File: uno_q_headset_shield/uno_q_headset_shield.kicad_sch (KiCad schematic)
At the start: 4 parts, among them J1 Power, J2 Digital/PWM, J3 Analog, J4 Digital/PWM

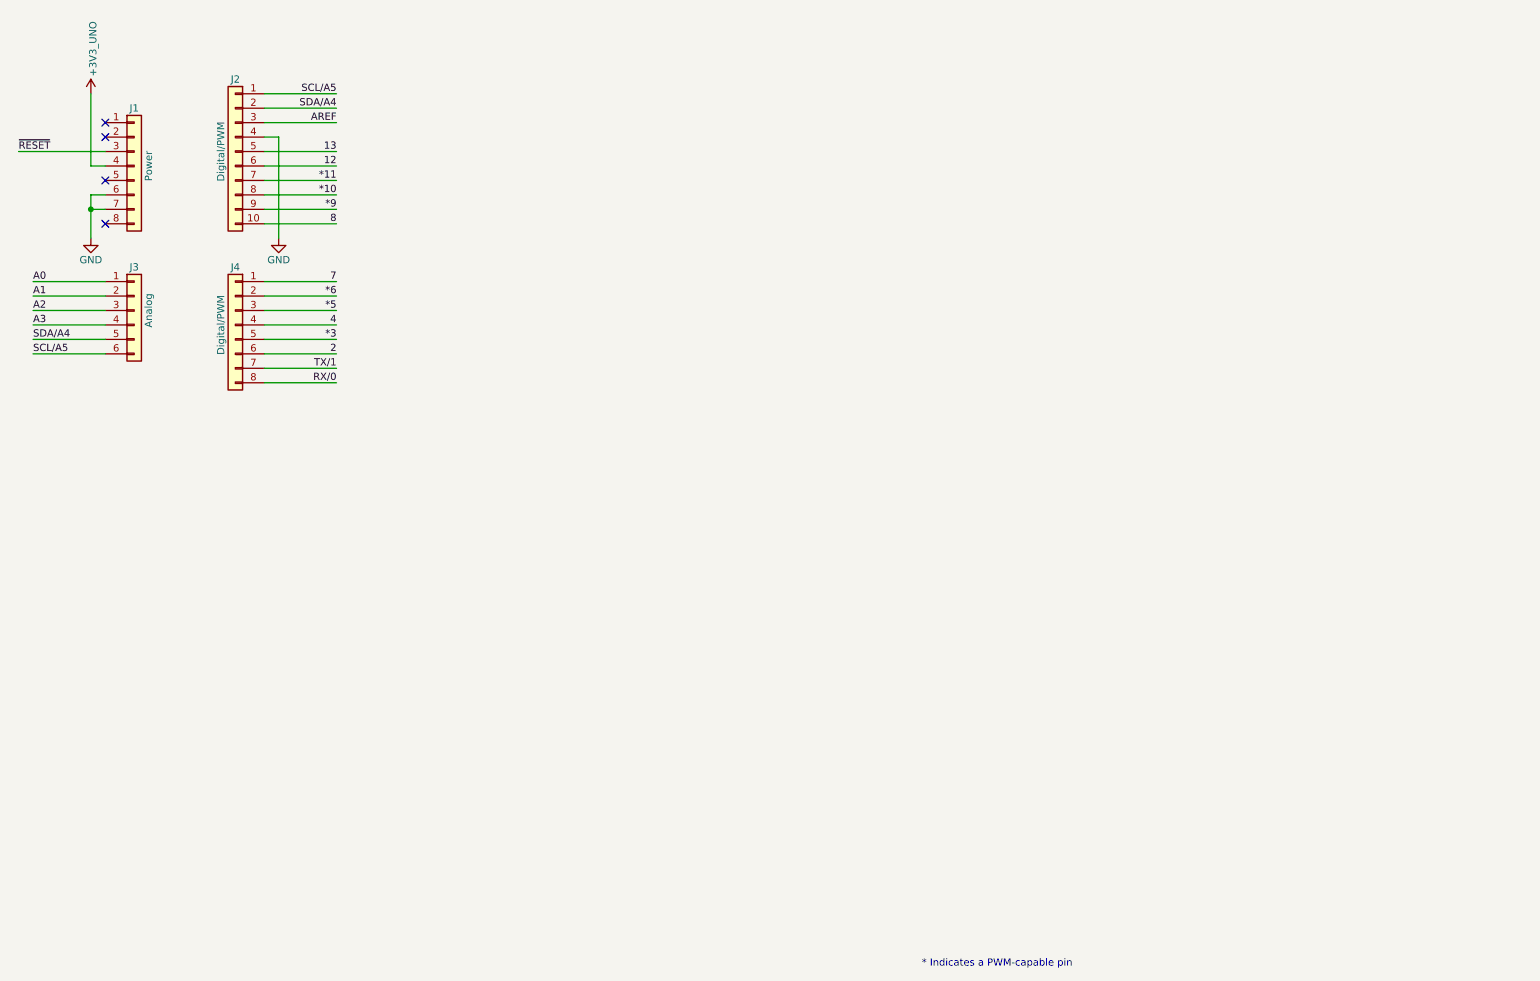
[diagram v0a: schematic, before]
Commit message: Full first pass at schematic (still need to finalize digital pin selection)
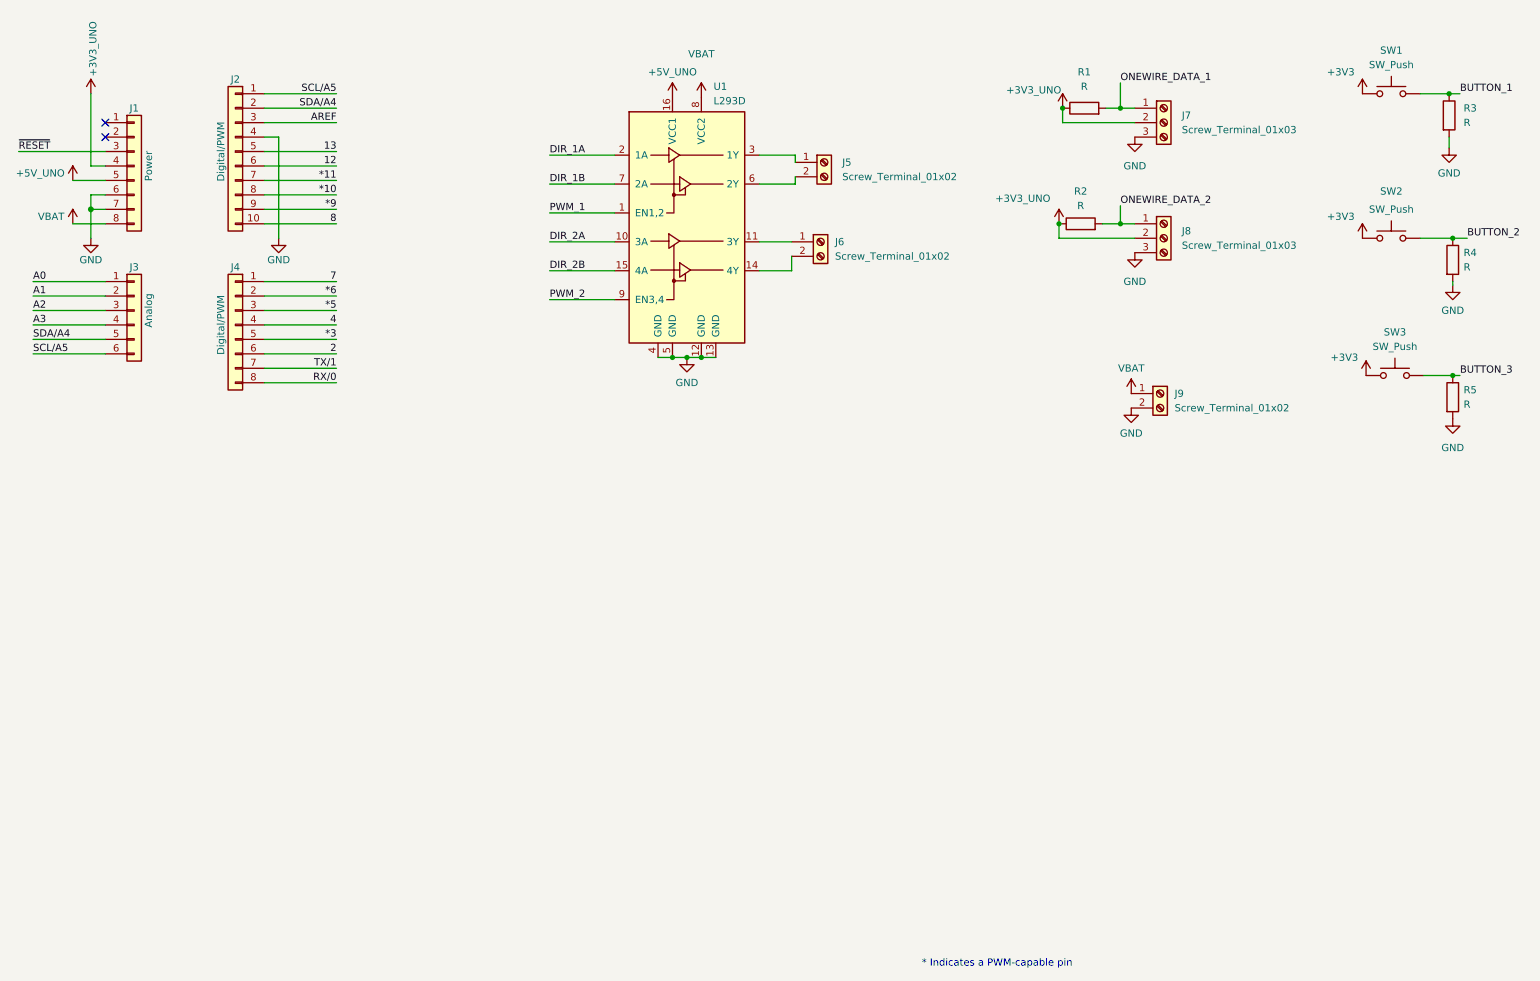
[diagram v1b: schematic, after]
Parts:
- added J5, J6, J9: Screw_Terminal_01x02, symbol Connector:Screw_Terminal_01x02
- added J7, J8: Screw_Terminal_01x03, symbol Connector:Screw_Terminal_01x03
- added R1, R2, R3, R4, R5: R, symbol Device:R
- added SW1, SW2, SW3: SW_Push, symbol Switch:SW_Push
- added U1: L293D, Package_DIP:DIP-16_W7.62mm, symbol Driver_Motor:L293D
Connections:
- net +3V3_UNO: now also J7.2 (Pin_2), J8.2 (Pin_2), R1.1, R2.1
- net GND: now also J7.3 (Pin_3), J8.3 (Pin_3), J9.2 (Pin_2), R3.2, R4.2, R5.2, U1.12 (GND), U1.13 (GND), U1.4 (GND), U1.5 (GND)
- net +5V_UNO: now reaches J1.5 (Pin_5)
- net +5V_UNO: now also U1.16 (VCC1)
- net VBAT: now reaches J1.8 (Pin_8)
- net VBAT: now also J9.1 (Pin_1), U1.8 (VCC2)
- new net: J5.1 (Pin_1), U1.3 (1Y)
- new net: J5.2 (Pin_2), U1.6 (2Y)
- new net: J6.1 (Pin_1), U1.11 (3Y)
- new net: J6.2 (Pin_2), U1.14 (4Y)
- new net +3V3: SW1.1, SW2.1, SW3.1
- new net BUTTON_1: R3.1, SW1.2
- new net BUTTON_2: R4.1, SW2.2
- new net BUTTON_3: R5.1, SW3.2
- new net DIR_1A: U1.2 (1A)
- new net DIR_1B: U1.7 (2A)
- new net DIR_2A: U1.10 (3A)
- new net DIR_2B: U1.15 (4A)
- new net ONEWIRE_DATA_1: J7.1 (Pin_1), R1.2
- new net ONEWIRE_DATA_2: J8.1 (Pin_1), R2.2
- new net PWM_1: U1.1 (EN1,2)
- new net PWM_2: U1.9 (EN3,4)
- no-connect marks 4 -> 2
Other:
- title: (none) -> The Headset - Uno Q Shield

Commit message: Shuffle pin constants, add (motor driver agnostic) labels in the schematic
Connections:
- net BUTTON_1 is gone; now on net A2: R3.1, SW1.2
- net BUTTON_2 is gone; now on net A3: R4.1, SW2.2
- net ONEWIRE_DATA_1 is gone; now on net *9: J7.1 (Pin_1), R1.2
- net ONEWIRE_DATA_2 is gone; now on net 12: J8.1 (Pin_1), R2.2
- net SDA/A4 is gone; now on net BUTTON_3: J2.2 (Pin_2), J3.5 (Pin_5)
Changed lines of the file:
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@@
-	(wire
-		(pts
-			(xy 62.23 39.37) (xy 74.93 39.37)
-		)
-		(stroke
-			(width 0)
-			(type solid)
-		)
-	)
 	(wire
 		(pts
@@
 	(wire
 		(pts
-			(xy 62.23 46.99) (xy 74.93 46.99)
-		)
-		(stroke
-			(width 0)
-			(type solid)
-		)
-	)
-	(wire
-		(pts
 			(xy 112.395 57.785) (xy 123.825 57.785)
 		)
@@
 	(wire
 		(pts
+			(xy 62.23 39.37) (xy 75.565 39.37)
+		)
+		(stroke
+			(width 0)
+			(type default)
+		)
+	)
+	(wire
+		(pts
 			(xy 155.575 42.545) (xy 149.225 42.545)
 		)
@@
 	(wire
 		(pts
-			(xy 34.29 64.77) (xy 21.59 64.77)
+			(xy 21.59 64.77) (xy 34.29 64.77)
 		)
 		(stroke
@@
 	(wire
 		(pts
+			(xy 62.23 46.99) (xy 75.565 46.99)
+		)
+		(stroke
+			(width 0)
+			(type default)
+		)
+	)
+	(wire
+		(pts
 			(xy 62.23 74.93) (xy 74.93 74.93)
 		)
@@
 	(wire
 		(pts
-			(xy 34.29 69.85) (xy 21.59 69.85)
+			(xy 17.78 69.85) (xy 34.29 69.85)
 		)
 		(stroke
@@
 		)
 	)
+	(label "ONEWIRE_DATA_1"
+		(at 75.565 46.99 0)
+		(effects
+			(font
+				(size 1.27 1.27)
+			)
+			(justify left bottom)
+		)
+	)
 	(label "2"
 		(at 74.93 72.39 180)
@@
 		)
 	)
+	(label "ONEWIRE_DATA_2"
+		(at 75.565 39.37 0)
+		(effects
+			(font
+				(size 1.27 1.27)
+			)
+			(justify left bottom)
+		)
+	)
 	(label "A3"
 		(at 21.59 67.31 0)
@@
 		)
 	)
+	(label "BUTTON_2"
+		(at 26.035 67.31 0)
+		(effects
+			(font
+				(size 1.27 1.27)
+			)
+			(justify left bottom)
+		)
+	)
 	(label "*10"
 		(at 74.93 44.45 180)
@@
 		)
 	)
+	(label "BUTTON_3"
+		(at 25.4 69.85 0)
+		(effects
+			(font
+				(size 1.27 1.27)
+			)
+			(justify left bottom)
+		)
+	)
+	(label "BUTTON_1"
+		(at 25.4 64.77 0)
+		(effects
+			(font
+				(size 1.27 1.27)
+			)
+			(justify left bottom)
+		)
+	)
 	(label "PWM_1"
 		(at 112.395 47.625 0)
@@
 	)
 	(label "SDA{slash}A4"
-		(at 21.59 69.85 0)
-		(effects
-			(font
+		(at 17.78 69.85 0)
+		(effects
+			(font

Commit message: two pwm labels
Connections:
- net PWM_1 is gone; now on net *5: U1.1 (EN1,2)
- net PWM_2 is gone; now on net *6: U1.9 (EN3,4)
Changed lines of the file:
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@@
+		)
+	)
+	(label "PWM_1"
+		(at 62.23 64.77 0)
+		(effects
+			(font
+				(size 1.27 1.27)
+			)
+			(justify left bottom)
 		)
 	)
@@
 		(effects
 			(font
+				(size 1.27 1.27)
+			)
+			(justify left bottom)
+		)
+	)
+	(label "PWM_2"
+		(at 62.23 62.23 0)
+		(effects
+			(font

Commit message: Schematic with DRV8874 + code fix
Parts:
- removed J9: Screw_Terminal_01x02, symbol Connector:Screw_Terminal_01x02
- removed U1: L293D, Package_DIP:DIP-16_W7.62mm, symbol Driver_Motor:L293D
- added J9: Screw_Terminal_01x03, symbol Connector:Screw_Terminal_01x03
- added JP1, JP2: SolderJumper_3_Open, symbol Jumper:SolderJumper_3_Open
- added U1, U2: Pololu_DRV8874_Carrier_4035, symbol New_Library:Pololu_DRV8874_Carrier_#4035
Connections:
- net *10: now also U2.4 (PH/IN2)
- net *11: now also U1.13 (~{FAULT}), U2.13 (~{FAULT})
- net *3: now also U1.3 (EN/IN1)
- net *5: now also U1.4 (PH/IN2)
- net *6: now also U2.3 (EN/IN1)
- net +3V3_UNO: now also JP1.1 (A), JP2.1 (A)
- net 4: now also U1.6 (~{SLEEP}), U2.6 (~{SLEEP})
- net A0: now also U1.14 (CS)
- net A1: now also U2.14 (CS)
- net GND: now also J9.2 (Pin_2), JP1.3 (B), JP2.3 (B), U1.2 (GND), U1.9 (GND), U2.2 (GND), U2.9 (GND)
- net at J5.1 (Pin_1): now also U1.10 (OUT1)
- net at J5.2 (Pin_2): now also U1.11 (OUT2)
- net at J6.1 (Pin_1): now also U2.10 (OUT1)
- net at J6.2 (Pin_2): now also U2.11 (OUT2)
- net VBAT renamed VBAT_1
- net VBAT_1: now also J9.1 (Pin_1)
- new net PMODE_1: JP1.2 (C), U1.5 (PMODE)
- new net PMODE_2: JP2.2 (C), U2.5 (PMODE)
- new net VBAT_2: J9.3 (Pin_3), U1.8 (VIN), U2.8 (VIN)
- no-connect marks 2 -> 8
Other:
- moved on the sheet: J6

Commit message: Create footprint for DRV8874 carrier, assign footprints
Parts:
- J5, J6: footprint (none) -> TerminalBlock_Phoenix:TerminalBlock_Phoenix_MKDS-1,5-2-5.08_1x02_P5.08mm_Horizontal
- J7, J8, J9: footprint (none) -> TerminalBlock_Phoenix:TerminalBlock_Phoenix_MKDS-1,5-3-5.08_1x03_P5.08mm_Horizontal
- JP1, JP2: footprint (none) -> Jumper:SolderJumper-3_P2.0mm_Open_TrianglePad1.0x1.5mm_NumberLabels
- R1, R2, R3, R4, R5: footprint (none) -> Resistor_SMD:R_1206_3216Metric_Pad1.30x1.75mm_HandSolder
- SW1, SW2, SW3: footprint (none) -> Button_Switch_SMD:SW_Push_1P1T_NO_CK_KSC6xxJ
- U1, U2: footprint (none) -> DRV887X_Carrier:DRV887X_Carrier
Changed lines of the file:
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@@
 			)
 		)
-		(property "Footprint" ""
+		(property "Footprint" "DRV887X_Carrier:DRV887X_Carrier"
 			(at 132.715 41.275 0)
 			(hide yes)
@@
 			)
 		)
-		(property "Footprint" ""
+		(property "Footprint" "Resistor_SMD:R_1206_3216Metric_Pad1.30x1.75mm_HandSolder"
 			(at 269.367 80.01 90)
 			(hide yes)
@@
 			)
 		)
-		(property "Footprint" ""
+		(property "Footprint" "TerminalBlock_Phoenix:TerminalBlock_Phoenix_MKDS-1,5-3-5.08_1x03_P5.08mm_Horizontal"
 			(at 220.345 31.75 0)
 			(hide yes)
@@
 			)
 		)
-		(property "Footprint" ""
+		(property "Footprint" "TerminalBlock_Phoenix:TerminalBlock_Phoenix_MKDS-1,5-2-5.08_1x02_P5.08mm_Horizontal"
 			(at 160.655 38.735 0)
 			(hide yes)
@@
 			)
 		)
-		(property "Footprint" ""
+		(property "Footprint" "Resistor_SMD:R_1206_3216Metric_Pad1.30x1.75mm_HandSolder"
 			(at 206.375 30.988 90)
 			(hide yes)
@@
 			)
 		)
-		(property "Footprint" ""
+		(property "Footprint" "Button_Switch_SMD:SW_Push_1P1T_NO_CK_KSC6xxJ"
 			(at 260.35 46.99 0)
 			(hide yes)
@@
 			)
 		)
-		(property "Footprint" ""
+		(property "Footprint" "Button_Switch_SMD:SW_Push_1P1T_NO_CK_KSC6xxJ"
 			(at 260.35 21.59 0)
 			(hide yes)
@@
 			)
 		)
-		(property "Footprint" ""
+		(property "Footprint" "TerminalBlock_Phoenix:TerminalBlock_Phoenix_MKDS-1,5-3-5.08_1x03_P5.08mm_Horizontal"
 			(at 221.615 81.915 0)
 			(hide yes)
@@
 			)
 		)
-		(property "Footprint" ""
+		(property "Footprint" "TerminalBlock_Phoenix:TerminalBlock_Phoenix_MKDS-1,5-2-5.08_1x02_P5.08mm_Horizontal"
 			(at 160.02 86.995 0)
 			(hide yes)
@@
 			)
 		)
-		(property "Footprint" ""
+		(property "Footprint" "Button_Switch_SMD:SW_Push_1P1T_NO_CK_KSC6xxJ"
 			(at 260.985 71.12 0)
 			(hide yes)
@@
 			)
 		)
-		(property "Footprint" ""
+		(property "Footprint" "Resistor_SMD:R_1206_3216Metric_Pad1.30x1.75mm_HandSolder"
 			(at 269.367 55.88 90)
 			(hide yes)
@@
 			)
 		)
-		(property "Footprint" ""
+		(property "Footprint" "DRV887X_Carrier:DRV887X_Carrier"
 			(at 132.715 90.805 0)
 			(hide yes)
@@
 			)
 		)
-		(property "Footprint" ""
+		(property "Footprint" "TerminalBlock_Phoenix:TerminalBlock_Phoenix_MKDS-1,5-3-5.08_1x03_P5.08mm_Horizontal"
 			(at 220.345 52.07 0)
 			(hide yes)
@@
 			)
 		)
-		(property "Footprint" ""
+		(property "Footprint" "Resistor_SMD:R_1206_3216Metric_Pad1.30x1.75mm_HandSolder"
 			(at 205.74 51.308 90)
 			(hide yes)
@@
 			)
 		)
-		(property "Footprint" ""
+		(property "Footprint" "Jumper:SolderJumper-3_P2.0mm_Open_TrianglePad1.0x1.5mm_NumberLabels"
 			(at 97.155 65.405 0)
 			(hide yes)
@@
 			)
 		)
-		(property "Footprint" ""
+		(property "Footprint" "Resistor_SMD:R_1206_3216Metric_Pad1.30x1.75mm_HandSolder"
 			(at 268.732 30.48 90)
 			(hide yes)
@@
 			)
 		)
-		(property "Footprint" ""
+		(property "Footprint" "Jumper:SolderJumper-3_P2.0mm_Open_TrianglePad1.0x1.5mm_NumberLabels"
 			(at 96.52 116.84 0)
 			(hide yes)
